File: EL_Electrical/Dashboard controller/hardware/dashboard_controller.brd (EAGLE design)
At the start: 67.1 x 54.5 mm, 46 parts, among them IC1 MCP2562-E_SN, IC2 MCP2515-I_SO, J1 22-27-2091-09, Q1 BSS138, Q4 BSS138, Q5 BSS138, Q6 BSS138

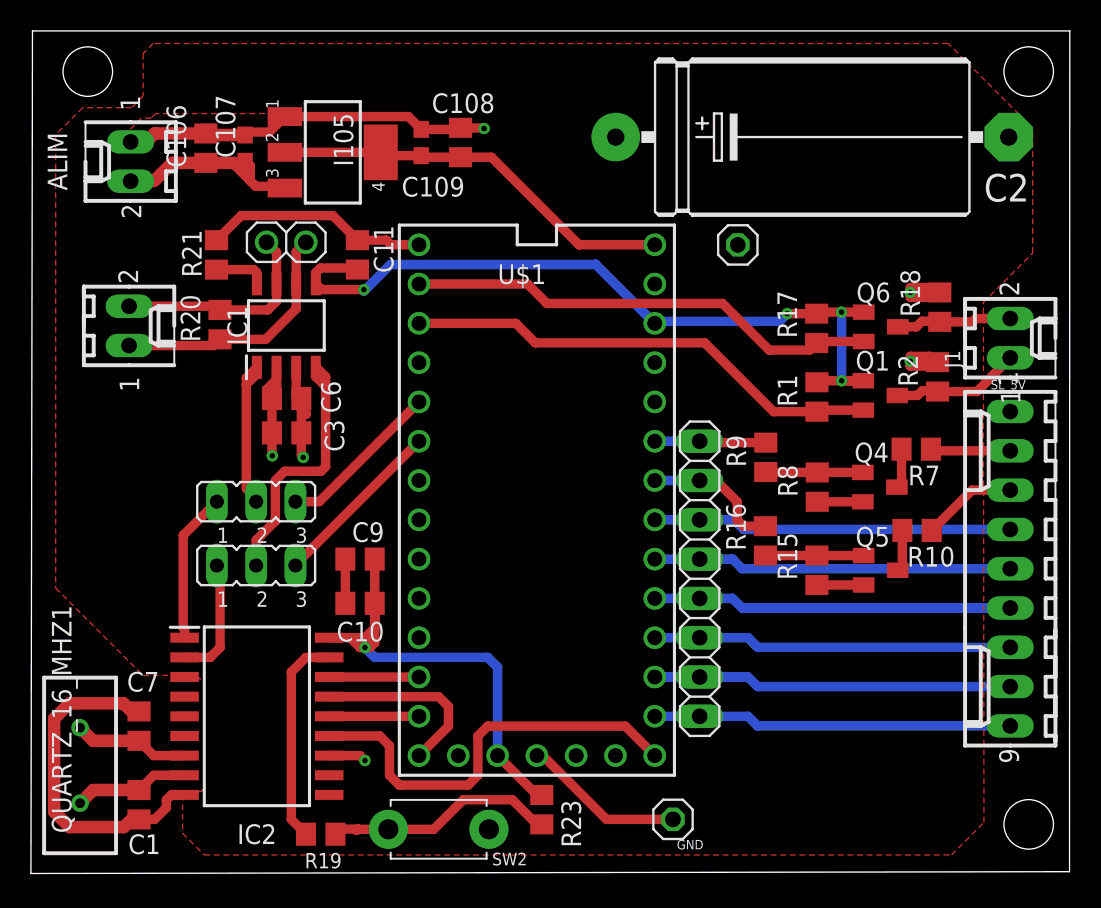
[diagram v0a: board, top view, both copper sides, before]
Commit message: Update holes and text
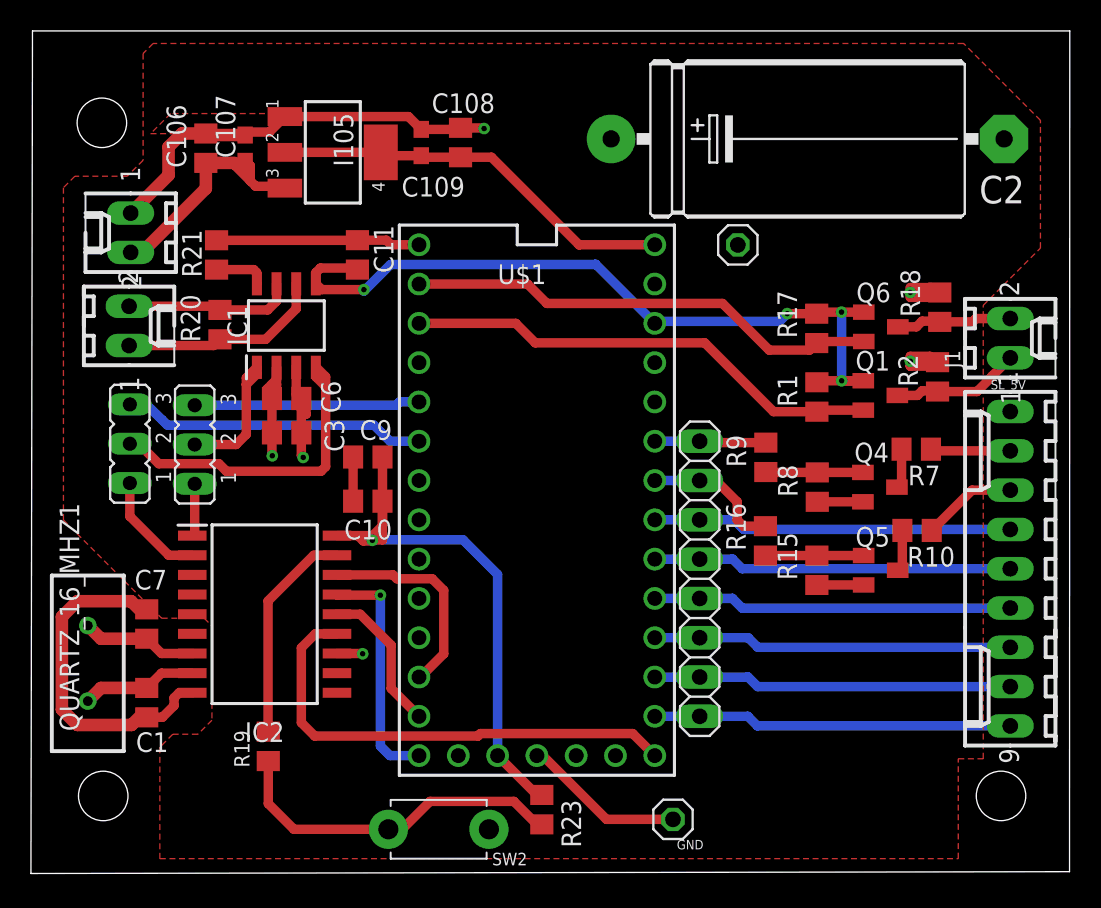
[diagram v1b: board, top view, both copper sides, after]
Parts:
- removed ALIM: 22-27-2021-02, con-molex:6410-02
- removed TEST_CAN: (no value), test_pin_DTA:1X02
- added POWER: 22-27-2021-02, con-molex:6410-02
- moved J_RX_CAN 11.3 mm to (6.39, 27.8), turned to 90 degrees
- moved C10 6.62 mm to (21.8, 24.1)
- moved C9 6.62 mm to (21.8, 26.9)
- moved IC2 6.62 mm to (15.1, 16.8)
- moved QUARTZ_16_MHZ1 6.62 mm to (3.67, 13.6)
- moved C1 6.62 mm to (7.49, 11.0)
- moved C7 6.62 mm to (7.49, 16.1)
- moved R19 6.61 mm to (15.3, 8.22), turned to 270 degrees
- moved J_TX_CAN 5.42 mm to (10.6, 27.7), turned to 90 degrees
- moved C2 0.32 mm to (50.2, 47.5)
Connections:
- net +12V: now also POWER.2; no longer ALIM.2
- net GND: now also POWER.1; no longer ALIM.1
- net N$1: no longer TEST_CAN.1
- net N$6: no longer TEST_CAN.2
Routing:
- net INT: track 38.9 -> 28.1 mm
- net CAN-RX_HARDWARE: track 11.3 -> 19.7 mm
- net +12V: track 49.5 -> 57.8 mm
- net CS: track 5.80 -> 13.6 mm
- net RESET: track 15.1 -> 22.5 mm
- net CAN-TXD-SOFTWARE: track 9.73 -> 3.41 mm
- net +3V3: track 82.3 -> 88.0 mm
- net SCK: track 27.3 -> 31.4 mm
- net CAN-TX_HARDWARE: track 10.7 -> 14.6 mm
- net RX_CAN: track 17.8 -> 21.7 mm
- net SI: track 5.80 -> 9.68 mm
- net SO: track 11.9 -> 15.3 mm, vias 0 -> 1
- net N$1: track 13.9 -> 11.0 mm
- net N$6: track 16.3 -> 13.4 mm
- net GND: track 88.6 -> 90.3 mm
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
